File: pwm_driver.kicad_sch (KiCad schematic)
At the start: 40 parts, among them J1 V_{In}, J2 GND_{In}, J3 SolderPad, J4 SolderPad, Q1 BC817, Q2 BC807, Q3 BUK7880-55A, U1 TLV2372, U2 LM393

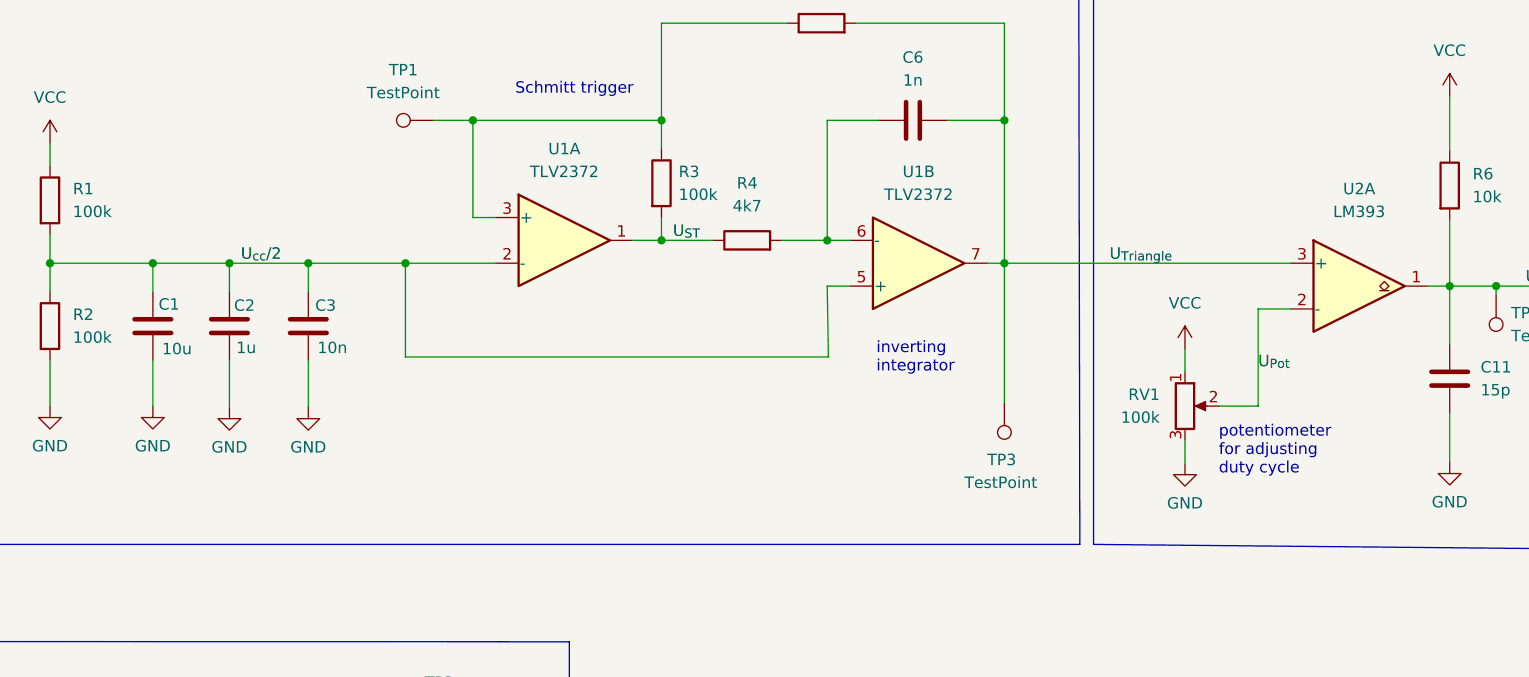
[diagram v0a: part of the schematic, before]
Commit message: minor redesign (decoupling cap)
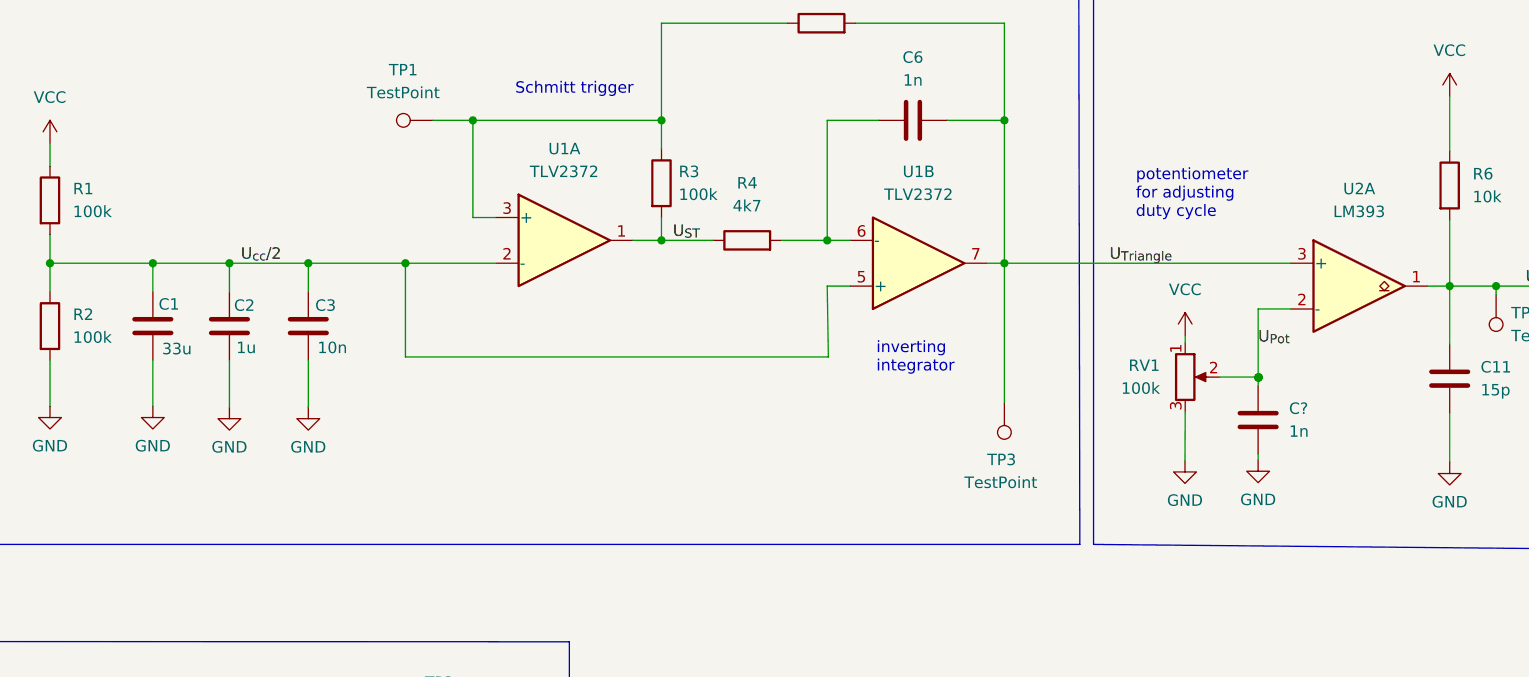
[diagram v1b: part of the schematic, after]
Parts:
- added C?: 1n, Capacitor_SMD:C_1206_3216Metric_Pad1.33x1.80mm_HandSolder, symbol Device:C
- C1: value 10u -> 33u
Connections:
- net GND: now also C?.2
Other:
- moved on the sheet: RV1
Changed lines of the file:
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@@
     (title "PWM power output generator")
     (date "2022-01-15")
-    (rev "1.1")
+    (rev "1.2")
     (comment 1 "Frank Kirschbaum")
     (comment 4 "PWM power output generator")
@@
   (junction (at 40.259 57.404) (diameter 0) (color 0 0 0 0)
   )
+  (junction (at 163.0934 70.1294) (diameter 0) (color 0 0 0 0)
+  )
+  (junction (at 163.1442 70.0786) (diameter 0) (color 0 0 0 0)
+  )
   (junction (at 115.189 54.864) (diameter 0) (color 0 0 0 0)
   )
@@
   )
   (junction (at 175.7934 115.951) (diameter 0) (color 0 0 0 0)
+  )
+  (junction (at 163.0934 70.0786) (diameter 0) (color 0 0 0 0)
   )
   (junction (at 96.774 41.529) (diameter 0) (color 0 0 0 0)
@@
     (stroke (width 0) (type default) (color 0 0 0 0))
   )
-  (wire (pts (xy 154.94 77.089) (xy 154.94 79.629))
+  (wire (pts (xy 154.9654 73.8632) (xy 154.94 79.3242))
     (stroke (width 0) (type default) (color 0 0 0 0))
   )
@@
     (stroke (width 0) (type default) (color 0 0 0 0))
   )
+  (wire (pts (xy 163.0934 70.0786) (xy 163.1442 70.0786))
+    (stroke (width 0) (type default) (color 0 0 0 0))
+  )
   (wire (pts (xy 49.53 115.57) (xy 54.6354 115.5192))
     (stroke (width 0) (type default) (color 0 0 0 0))
@@
     (stroke (width 0) (type default) (color 0 0 0 0))
   )
-  (wire (pts (xy 163.068 62.484) (xy 163.068 73.279))
+  (wire (pts (xy 163.068 62.484) (xy 163.068 70.0532))
     (stroke (width 0) (type default) (color 0 0 0 0))
   )
@@
     (stroke (width 0) (type default) (color 0 0 0 0))
   )
+  (wire (pts (xy 163.068 78.6384) (xy 163.068 79.248))
+    (stroke (width 0) (type default) (color 0 0 0 0))
+  )
   (wire (pts (xy 146.2024 116.205) (xy 146.2024 118.11))
     (stroke (width 0) (type default) (color 0 0 0 0))
@@
     (stroke (width 0) (type default) (color 0 0 0 0))
   )
-  (wire (pts (xy 154.94 66.929) (xy 154.94 69.469))
+  (wire (pts (xy 163.0934 70.1294) (xy 163.0934 70.0786))
+    (stroke (width 0) (type default) (color 0 0 0 0))
+  )
+  (wire (pts (xy 154.9654 65.4304) (xy 154.9654 66.2432))
     (stroke (width 0) (type default) (color 0 0 0 0))
   )
@@
     (stroke (width 0) (type default) (color 0 0 0 0))
   )
-  (wire (pts (xy 158.75 73.279) (xy 163.068 73.279))
+  (wire (pts (xy 158.7754 70.0532) (xy 163.068 70.0532))
     (stroke (width 0) (type default) (color 0 0 0 0))
   )
@@
   )
   (wire (pts (xy 181.9148 59.944) (xy 184.3532 59.944))
+    (stroke (width 0) (type default) (color 0 0 0 0))
+  )
+  (wire (pts (xy 163.068 71.0184) (xy 163.0934 70.1294))
     (stroke (width 0) (type default) (color 0 0 0 0))
   )
@@
     (effects (font (size 1.27 1.27)) (justify left bottom))
   )
-  (text "potentiometer\nfor adjusting\nduty cycle" (at 158.6992 81.0514 0)
+  (text "potentiometer\nfor adjusting\nduty cycle" (at 149.479 52.5526 0)
     (effects (font (size 1.27 1.27)) (justify left bottom))
   )
@@
     (effects (font (size 1.27 1.27)) (justify left bottom))
   )
-  (label "U_{Pot}" (at 163.068 69.342 0)
+  (label "U_{Pot}" (at 163.068 66.5988 0)
     (effects (font (size 1.27 1.27)) (justify left bottom))
   )
@@
     (pin "2")
   )
+  (symbol (lib_id "power:GND") (at 163.068 79.248 0) (unit 1)
+    (in_bom yes) (on_board yes) (fields_autoplaced)
+    (property "Reference" "#PWR?" (id 0) (at 163.068 85.598 0)
+      (effects (font (size 1.27 1.27)) hide)
+    )
+    (property "Value" "GND" (id 1) (at 163.068 83.693 0))
+    (property "Footprint" "" (id 2) (at 163.068 79.248 0)
+      (effects (font (size 1.27 1.27)) hide)
+    )
+    (property "Datasheet" "" (id 3) (at 163.068 79.248 0)
+      (effects (font (size 1.27 1.27)) hide)
+    )
+    (pin "1")
+  )
   (symbol (lib_id "Device:R") (at 96.774 48.514 0) (unit 1)
     (in_bom yes) (on_board yes) (fields_autoplaced)
@@
       (effects (font (size 1.27 1.27)) (justify left))
     )
-    (property "Value" "10u" (id 1) (at 41.275 66.929 0)
+    (property "Value" "33u" (id 1) (at 41.275 66.929 0)
       (effects (font (size 1.27 1.27)) (justify left))
     )
@@
     (pin "2")
   )
-  (symbol (lib_id "Device:R_Potentiometer") (at 154.94 73.279 0) (unit 1)
-    (in_bom yes) (on_board yes) (fields_autoplaced)
-    (property "Reference" "RV1" (id 0) (at 152.146 72.0089 0)
+  (symbol (lib_id "Device:R_Potentiometer") (at 154.9654 70.0532 0) (unit 1)
+    (in_bom yes) (on_board yes) (fields_autoplaced)
+    (property "Reference" "RV1" (id 0) (at 152.1714 68.7831 0)
       (effects (font (size 1.27 1.27)) (justify right))
     )
-    (property "Value" "100k" (id 1) (at 152.146 74.5489 0)
+    (property "Value" "100k" (id 1) (at 152.1714 71.3231 0)
       (effects (font (size 1.27 1.27)) (justify right))
     )
-    (property "Footprint" "Connector_PinHeader_2.54mm:PinHeader_1x03_P2.54mm_Vertical_SMD_Pin1Left" (id 2) (at 154.94 73.279 0)
-      (effects (font (size 1.27 1.27)) hide)
-    )
-    (property "Datasheet" "~" (id 3) (at 154.94 73.279 0)
+    (property "Footprint" "Connector_PinHeader_2.54mm:PinHeader_1x03_P2.54mm_Vertical_SMD_Pin1Left" (id 2) (at 154.9654 70.0532 0)
+      (effects (font (size 1.27 1.27)) hide)
+    )
+    (property "Datasheet" "~" (id 3) (at 154.9654 70.0532 0)
       (effects (font (size 1.27 1.27)) hide)
     )
@@
     )
     (pin "1")
+  )
+  (symbol (lib_id "Device:C") (at 163.068 74.8284 0) (unit 1)
+    (in_bom yes) (on_board yes) (fields_autoplaced)
+    (property "Reference" "C?" (id 0) (at 166.497 73.5583 0)
+      (effects (font (size 1.27 1.27)) (justify left))
+    )
+    (property "Value" "1n" (id 1) (at 166.497 76.0983 0)
+      (effects (font (size 1.27 1.27)) (justify left))
+    )
+    (property "Footprint" "Capacitor_SMD:C_1206_3216Metric_Pad1.33x1.80mm_HandSolder" (id 2) (at 164.0332 78.6384 0)
+      (effects (font (size 1.27 1.27)) hide)
+    )
+    (property "Datasheet" "~" (id 3) (at 163.068 74.8284 0)
+      (effects (font (size 1.27 1.27)) hide)
+    )
+    (pin "1")
+    (pin "2")
   )
   (symbol (lib_id "Amplifier_Operational:TLV2372") (at 125.349 57.404 0) (mirror x) (unit 2)
@@
     (pin "1")
   )
-  (symbol (lib_id "power:VCC") (at 154.94 66.929 0) (unit 1)
-    (in_bom yes) (on_board yes) (fields_autoplaced)
-    (property "Reference" "#PWR012" (id 0) (at 154.94 70.739 0)
-      (effects (font (size 1.27 1.27)) hide)
-    )
-    (property "Value" "VCC" (id 1) (at 154.94 61.849 0))
-    (property "Footprint" "" (id 2) (at 154.94 66.929 0)
-      (effects (font (size 1.27 1.27)) hide)
-    )
-    (property "Datasheet" "" (id 3) (at 154.94 66.929 0)
+  (symbol (lib_id "power:VCC") (at 154.9654 65.4304 0) (unit 1)
+    (in_bom yes) (on_board yes) (fields_autoplaced)
+    (property "Reference" "#PWR012" (id 0) (at 154.9654 69.2404 0)
+      (effects (font (size 1.27 1.27)) hide)
+    )
+    (property "Value" "VCC" (id 1) (at 154.9654 60.3504 0))
+    (property "Footprint" "" (id 2) (at 154.9654 65.4304 0)
+      (effects (font (size 1.27 1.27)) hide)
+    )
+    (property "Datasheet" "" (id 3) (at 154.9654 65.4304 0)
       (effects (font (size 1.27 1.27)) hide)
     )
@@
     (pin "2")
   )
-  (symbol (lib_id "power:GND") (at 154.94 79.629 0) (unit 1)
-    (in_bom yes) (on_board yes) (fields_autoplaced)
-    (property "Reference" "#PWR013" (id 0) (at 154.94 85.979 0)
-      (effects (font (size 1.27 1.27)) hide)
-    )
-    (property "Value" "GND" (id 1) (at 154.94 84.074 0))
-    (property "Footprint" "" (id 2) (at 154.94 79.629 0)
-      (effects (font (size 1.27 1.27)) hide)
-    )
-    (property "Datasheet" "" (id 3) (at 154.94 79.629 0)
+  (symbol (lib_id "power:GND") (at 154.94 79.3242 0) (unit 1)
+    (in_bom yes) (on_board yes) (fields_autoplaced)
+    (property "Reference" "#PWR013" (id 0) (at 154.94 85.6742 0)
+      (effects (font (size 1.27 1.27)) hide)
+    )
+    (property "Value" "GND" (id 1) (at 154.94 83.7692 0))
+    (property "Footprint" "" (id 2) (at 154.94 79.3242 0)
+      (effects (font (size 1.27 1.27)) hide)
+    )
+    (property "Datasheet" "" (id 3) (at 154.94 79.3242 0)
       (effects (font (size 1.27 1.27)) hide)
     )
@@
       (reference "#PWR025") (unit 1) (value "GND") (footprint "")
     )
+    (path "/1f0bb5d0-f2db-4b59-ae64-ed9996a626e5"
+      (reference "#PWR?") (unit 1) (value "GND") (footprint "")
+    )
     (path "/22cf0ffa-9a4f-4b23-9faf-93b97fa9335a"
-      (reference "C1") (unit 1) (value "10u") (footprint "Capacitor_SMD:C_1206_3216Metric_Pad1.33x1.80mm_HandSolder")
+      (reference "C1") (unit 1) (value "33u") (footprint "Capacitor_SMD:C_1206_3216Metric_Pad1.33x1.80mm_HandSolder")
     )
     (path "/637d5b97-3b49-4bf0-abc5-0c2edd930838"
@@
       (reference "C11") (unit 1) (value "15p") (footprint "Capacitor_SMD:C_1206_3216Metric_Pad1.33x1.80mm_HandSolder")
     )
+    (path "/8004d44a-47d2-482e-a5b8-4a70421324d5"
+      (reference "C?") (unit 1) (value "1n") (footprint "Capacitor_SMD:C_1206_3216Metric_Pad1.33x1.80mm_HandSolder")
+    )
     (path "/67ec138c-9feb-44a7-8407-16e5fec3e23a"

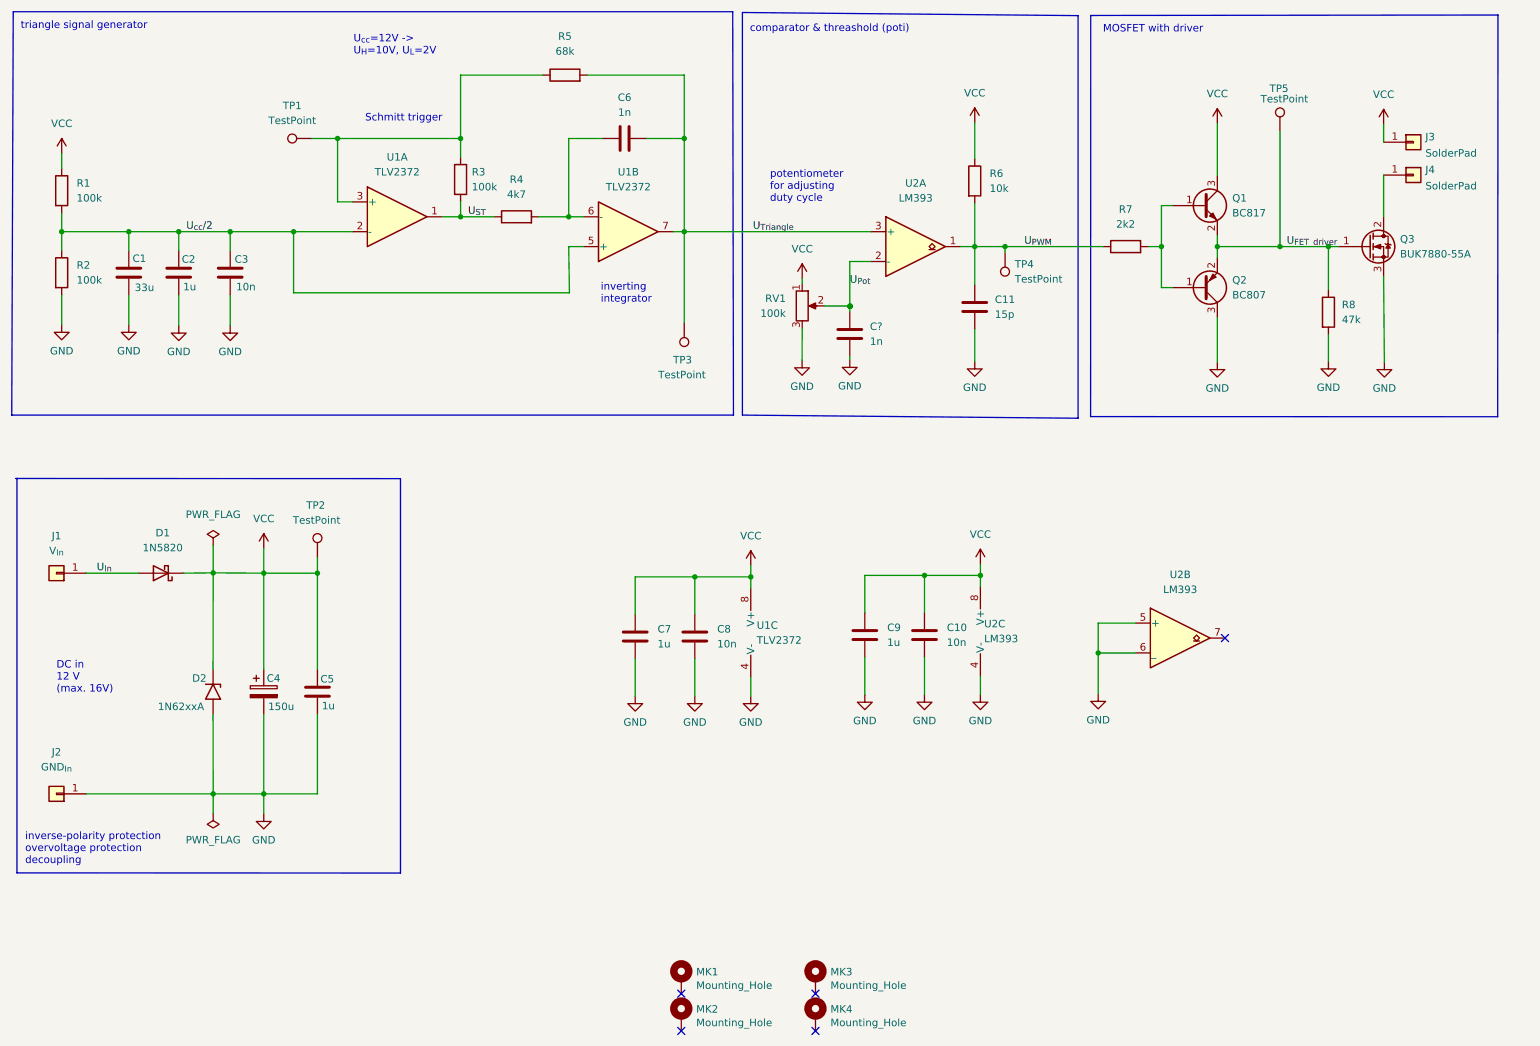
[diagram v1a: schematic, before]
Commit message: subfolder with simulation model added
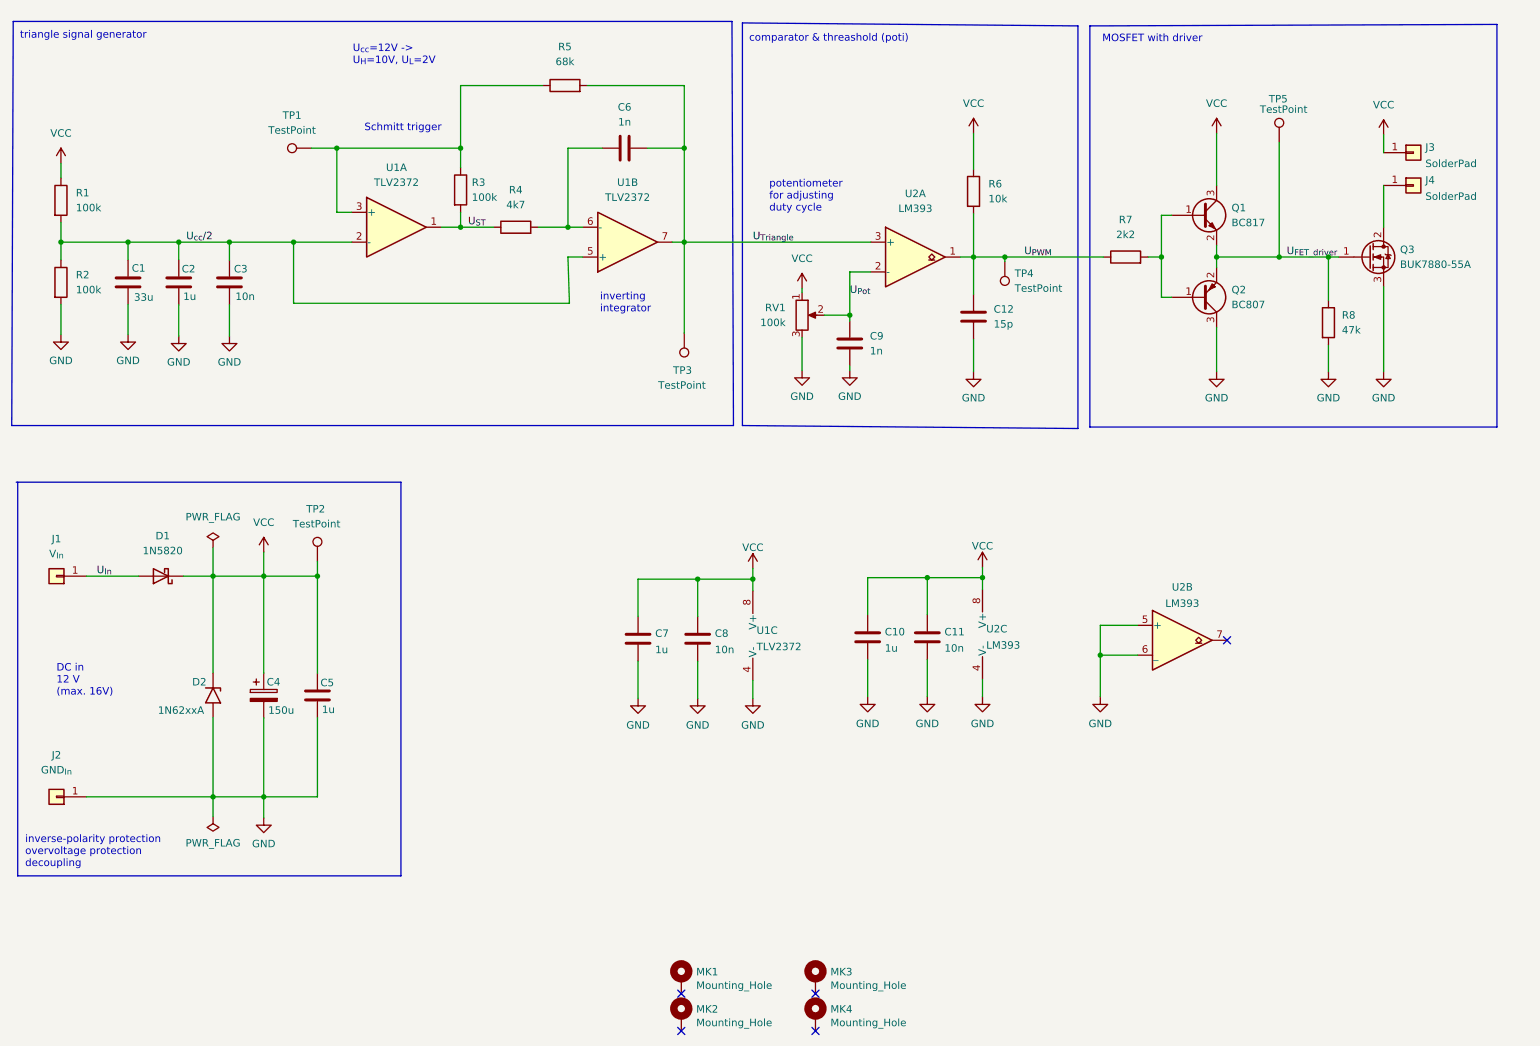
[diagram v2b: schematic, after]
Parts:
- gave numbers to parts that had none: 1
- renumbered C9 to C10, C10 to C11, C11 to C12
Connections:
- net U_{Pot}: now also C9.1
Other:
- moved on the sheet: C1, C10, C11, C12, C2, C3, C4, C5, C6, C7, C8, C9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

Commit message: photo added from working device
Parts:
- removed Q3: BUK7880-55A, Package_TO_SOT_SMD:SOT-223-3_TabPin2, symbol Transistor_FET:BUK7880-55A
- added Q3: TSM900N06CW_RPG, TRANS_TSM900N06CW_RPG:TRANS_TSM900N06CW_RPG, symbol TSM900N06CW_RPG:TSM900N06CW_RPG
- R1, R2: value 100k -> 51k
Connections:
- net GND: now also Q3.3
- net U_{FET_driver}: now also Q3.1
- net FET_Drain: now reaches J4.1 (Pin_1)
- net FET_Drain: now also Q3.2, Q3.4
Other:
- moved on the sheet: C1, C10, C11, C12, C2, C4, C5, C9, D1, D2, J1, J3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

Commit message: documentation edited
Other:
- company: (none) -> Ct Cherrytree
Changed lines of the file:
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@@
     (date "2022-01-15")
     (rev "1.2")
+    (company "Ct Cherrytree")
     (comment 1 "Frank Kirschbaum")
     (comment 4 "PWM power output generator")
